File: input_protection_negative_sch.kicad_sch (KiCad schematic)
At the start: 26 parts, among them Q3 SQM50020EL, Q4 SQM50020EL, U2 LM5067

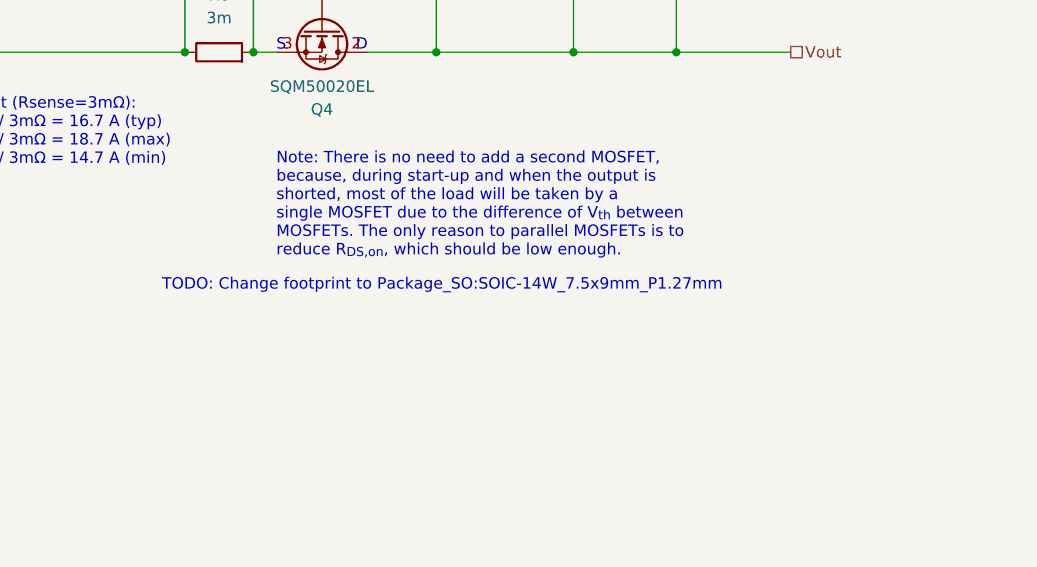
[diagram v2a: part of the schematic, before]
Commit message: Fixed LM5067 footprint
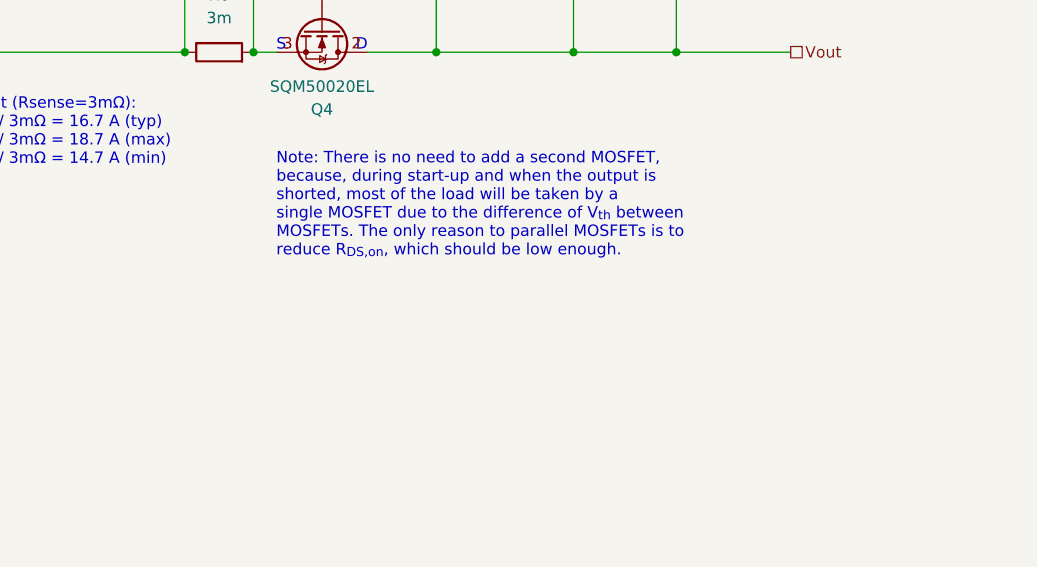
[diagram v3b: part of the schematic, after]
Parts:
- U2: footprint Package_SO:SOIC-14_3.9x8.7mm_P1.27mm -> Package_SO:SOIC-14W_7.5x9mm_P1.27mm
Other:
- note removed: "TODO: Change footprint to Package_SO:SOIC-14W_7.5x9mm_P1.27mm"
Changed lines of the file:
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@@
-    (effects (font (size 1.27 1.27)) (justify left bottom))
-  )
-  (text "TODO: Change footprint to Package_SO:SOIC-14W_7.5x9mm_P1.27mm"
-    (at 195.58 133.35 0)
     (effects (font (size 1.27 1.27)) (justify left bottom))
   )
@@
       (effects (font (size 1.27 1.27)))
     )
-    (property "Footprint" "Package_SO:SOIC-14_3.9x8.7mm_P1.27mm" (at 213.36 86.36 0)
-      (effects (font (size 1.27 1.27)) hide)
-    )
+    (property "Footprint" "Package_SO:SOIC-14W_7.5x9mm_P1.27mm" (at 213.36 86.36 0)
+      (effects (font (size 1.27 1.27)) hide)
+    )

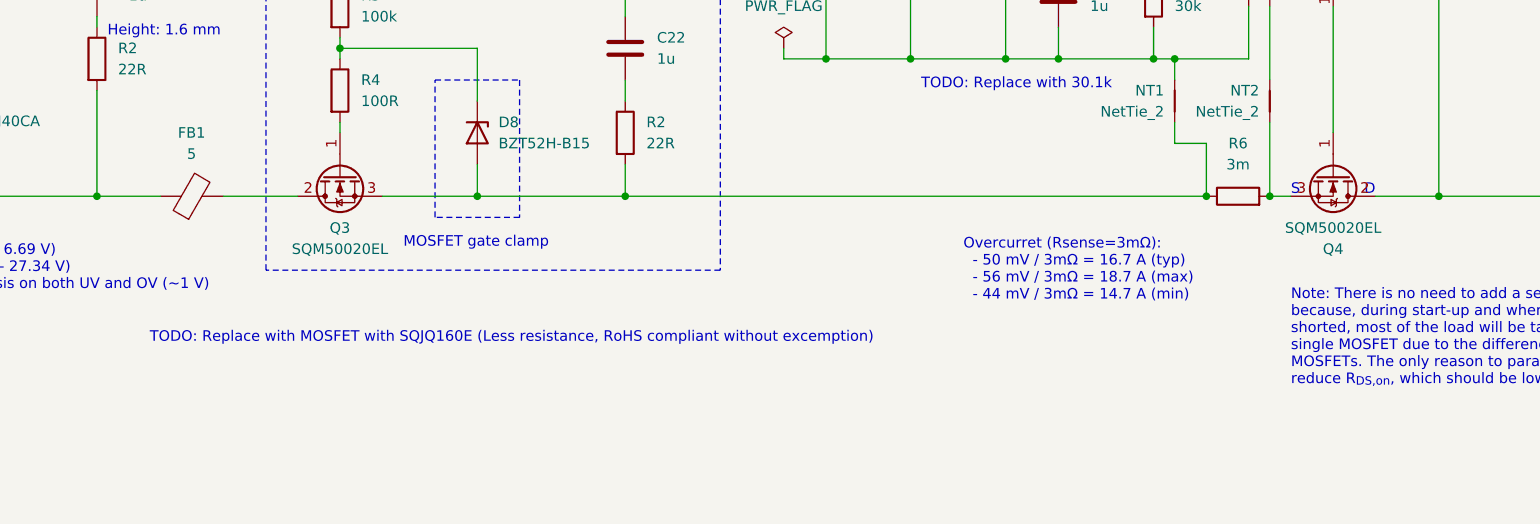
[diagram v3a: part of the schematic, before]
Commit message: Replace negative rail NMOS with SQJQ160E to reduce the on resistance
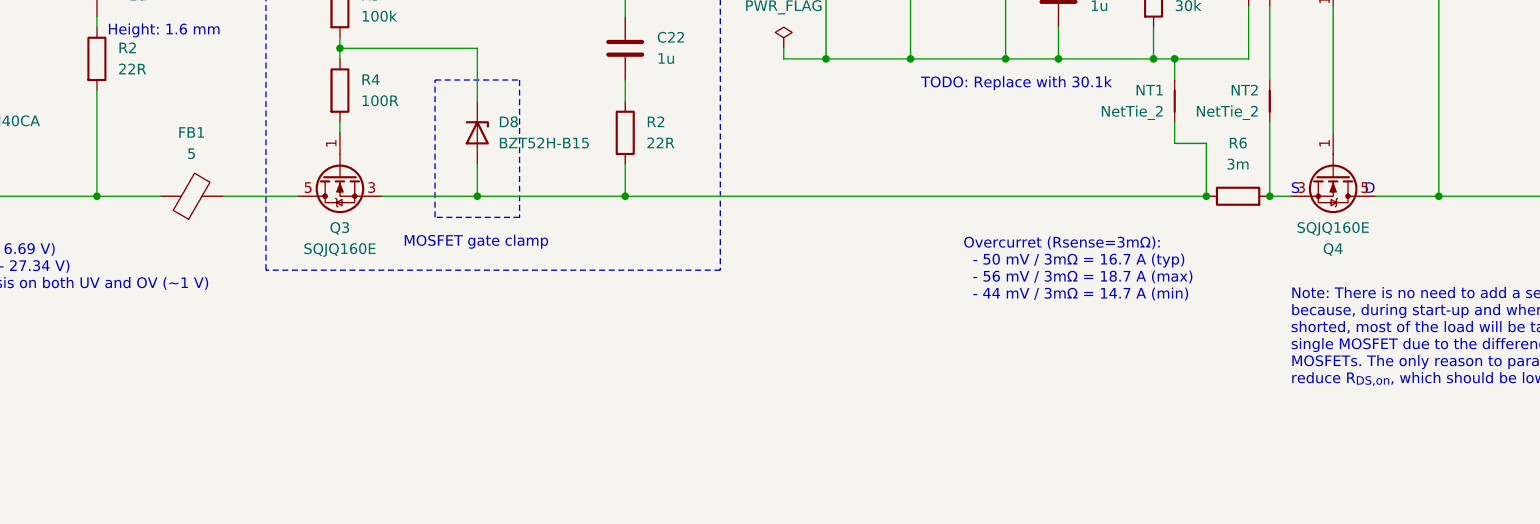
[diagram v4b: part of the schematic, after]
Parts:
- Q3, Q4: value SQM50020EL -> SQJQ160E; footprint Package_TO_SOT_SMD:TO-263-2 -> Package_SO:PowerPAK_SO-8L_Single; symbol Device:Q_NMOS_GDS -> Vishay:SQJQ160E; PN SQM50020EL -> SQJQ160E
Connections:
- net Vout: now also Q4.5 (D); no longer Q4.2 (D)
- net at NT2.1, Q4.3 (S), R6.2: now also Q4.2 (S), Q4.4 (S)
- net at D8.2 (A), NT1.1, Q3.3 (S)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: now also Q3.2 (S), Q3.4 (S)
- net at FB1.2: now also Q3.5 (D); no longer Q3.2 (D)
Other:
- note removed: "TODO: Replace with MOSFET with SQJQ160E (Less resistance, RoHS compliant without excemption)"
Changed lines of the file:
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@@
     (effects (font (size 1.27 1.27)) (justify right bottom))
-  )
-  (text "TODO: Replace with MOSFET with SQJQ160E (Less resistance, RoHS compliant without excemption)"
-    (at 71.12 124.46 0)
-    (effects (font (size 1.27 1.27)) (justify left bottom))
   )
   (text "Reverse polarity protection" (at 99.06 35.56 0)
@@
     (effects (font (size 1.27 1.27)) (justify right))
   )
-  (symbol (lib_id "Device:Q_NMOS_GDS") (at 213.36 104.14 270) (unit 1)
+  (symbol (lib_id "Vishay:SQJQ160E") (at 213.36 104.14 270) (unit 1)
     (in_bom yes) (on_board yes) (dnp no)
     (property "Reference" "Q4" (at 213.36 113.03 90)
       (effects (font (size 1.27 1.27)))
     )
-    (property "Value" "SQM50020EL" (at 213.36 110.49 90)
+    (property "Value" "SQJQ160E" (at 213.36 110.49 90)
       (effects (font (size 1.27 1.27)))
     )
-    (property "Footprint" "Package_TO_SOT_SMD:TO-263-2" (at 215.9 109.22 0)
+    (property "Footprint" "Package_SO:PowerPAK_SO-8L_Single" (at 215.9 109.22 0)
       (effects (font (size 1.27 1.27)) hide)
     )
@@
       (effects (font (size 1.27 1.27)) hide)
     )
-    (property "PN" "SQM50020EL" (at 213.36 104.14 0)
+    (property "PN" "SQJQ160E" (at 213.36 104.14 0)
       (effects (font (size 1.27 1.27)) hide)
     )
@@
     (pin "2")
     (pin "3")
+    (pin "3")
+    (pin "5")
+    (pin "4")
     (instances
       (project "main"
@@
     )
   )
-  (symbol (lib_id "Device:Q_NMOS_GDS") (at 93.98 104.14 90) (mirror x) (unit 1)
+  (symbol (lib_id "Vishay:SQJQ160E") (at 93.98 104.14 90) (mirror x) (unit 1)
     (in_bom yes) (on_board yes) (dnp no)
     (property "Reference" "Q3" (at 93.98 110.49 90)
       (effects (font (size 1.27 1.27)))
     )
-    (property "Value" "SQM50020EL" (at 93.98 113.03 90)
+    (property "Value" "SQJQ160E" (at 93.98 113.03 90)
       (effects (font (size 1.27 1.27)))
     )
-    (property "Footprint" "Package_TO_SOT_SMD:TO-263-2" (at 91.44 109.22 0)
+    (property "Footprint" "Package_SO:PowerPAK_SO-8L_Single" (at 91.44 109.22 0)
       (effects (font (size 1.27 1.27)) hide)
     )
@@
       (effects (font (size 1.27 1.27)) hide)
     )
-    (property "PN" "SQM50020EL" (at 93.98 104.14 0)
+    (property "PN" "SQJQ160E" (at 93.98 104.14 0)
       (effects (font (size 1.27 1.27)) hide)
     )
@@
     (pin "2")
     (pin "3")
-    (instances
-      (project "main"
+    (pin "3")
+    (pin "5")
+    (pin "4")
+    (instances
+      (project "main"

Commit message: Replaced negative side NMOS with SQJQ160E Reduced number of thermal spokes required to 1
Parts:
- renumbered C20 to C29, FB1 to FB2
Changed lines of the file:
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@@
         )
         (path "/b4ace06a-3ad4-479e-aaa4-d547ecf6903f/1acfc0a8-4adc-455e-9f2b-420811df0901"
-          (reference "C21") (unit 1)
+          (reference "C30") (unit 1)
         )
       )
@@
   (symbol (lib_id "Device:FerriteBead") (at 76.2 106.68 90) (unit 1)
     (in_bom yes) (on_board yes) (dnp no) (fields_autoplaced)
-    (property "Reference" "FB1" (at 76.1492 99.06 90)
+    (property "Reference" "FB2" (at 76.1492 99.06 90)
       (effects (font (size 1.27 1.27)))
     )
@@
       (project "main"
         (path "/b4ace06a-3ad4-479e-aaa4-d547ecf6903f/1acfc0a8-4adc-455e-9f2b-420811df0901"
-          (reference "FB1") (unit 1)
+          (reference "FB2") (unit 1)
         )
       )
@@
         )
         (path "/b4ace06a-3ad4-479e-aaa4-d547ecf6903f/1acfc0a8-4adc-455e-9f2b-420811df0901"
-          (reference "R3") (unit 1)
+          (reference "R12") (unit 1)
         )
       )
@@
         )
         (path "/b4ace06a-3ad4-479e-aaa4-d547ecf6903f/1acfc0a8-4adc-455e-9f2b-420811df0901"
-          (reference "C22") (unit 1)
+          (reference "C31") (unit 1)
         )
       )
@@
         )
         (path "/b4ace06a-3ad4-479e-aaa4-d547ecf6903f/1acfc0a8-4adc-455e-9f2b-420811df0901"
-          (reference "C4") (unit 1)
+          (reference "C18") (unit 1)
         )
       )
@@
   (symbol (lib_id "Device:C") (at 180.34 82.55 0) (unit 1)
     (in_bom yes) (on_board yes) (dnp no) (fields_autoplaced)
-    (property "Reference" "C20" (at 184.15 81.28 0)
+    (property "Reference" "C29" (at 184.15 81.28 0)
       (effects (font (size 1.27 1.27)) (justify left))
     )
@@
       (project "main"
         (path "/b4ace06a-3ad4-479e-aaa4-d547ecf6903f/1acfc0a8-4adc-455e-9f2b-420811df0901"
-          (reference "C20") (unit 1)
-        )
-      )
+          (reference "C29") (unit 1)
+        )
+      )

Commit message: Consolidated BOM
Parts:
- Q3, Q4: RoHS By exemption -> Yes
- R18: value 30k -> 30.1k; PN CRCW080530K0FKEA -> CRCW080530K1FKEA
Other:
- note removed: "TODO: Replace with 30.1k"
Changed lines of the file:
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@@
-    (effects (font (size 1.27 1.27)) (justify left bottom))
-  )
-  (text "TODO: Replace with 30.1k" (at 163.83 93.98 0)
     (effects (font (size 1.27 1.27)) (justify left bottom))
   )
@@
       (effects (font (size 1.27 1.27)) hide)
     )
-    (property "RoHS" "By exemption" (at 213.36 104.14 0)
+    (property "RoHS" "Yes" (at 213.36 104.14 0)
       (effects (font (size 1.27 1.27)) hide)
     )
@@
       (effects (font (size 1.27 1.27)) (justify left))
     )
-    (property "Value" "30k" (at 194.31 83.82 0)
+    (property "Value" "30.1k" (at 194.31 83.82 0)
       (effects (font (size 1.27 1.27)) (justify left))
     )
@@
       (effects (font (size 1.27 1.27)) hide)
     )
-    (property "PN" "CRCW080530K0FKEA" (at 191.77 82.55 0)
+    (property "PN" "CRCW080530K1FKEA" (at 191.77 82.55 0)
       (effects (font (size 1.27 1.27)) hide)
     )
@@
       (effects (font (size 1.27 1.27)) hide)
     )
-    (property "RoHS" "By exemption" (at 93.98 104.14 0)
-      (effects (font (size 1.27 1.27)) hide)
-    )
+    (property "RoHS" "Yes" (at 93.98 104.14 0)
+      (effects (font (size 1.27 1.27)) hide)
+    )

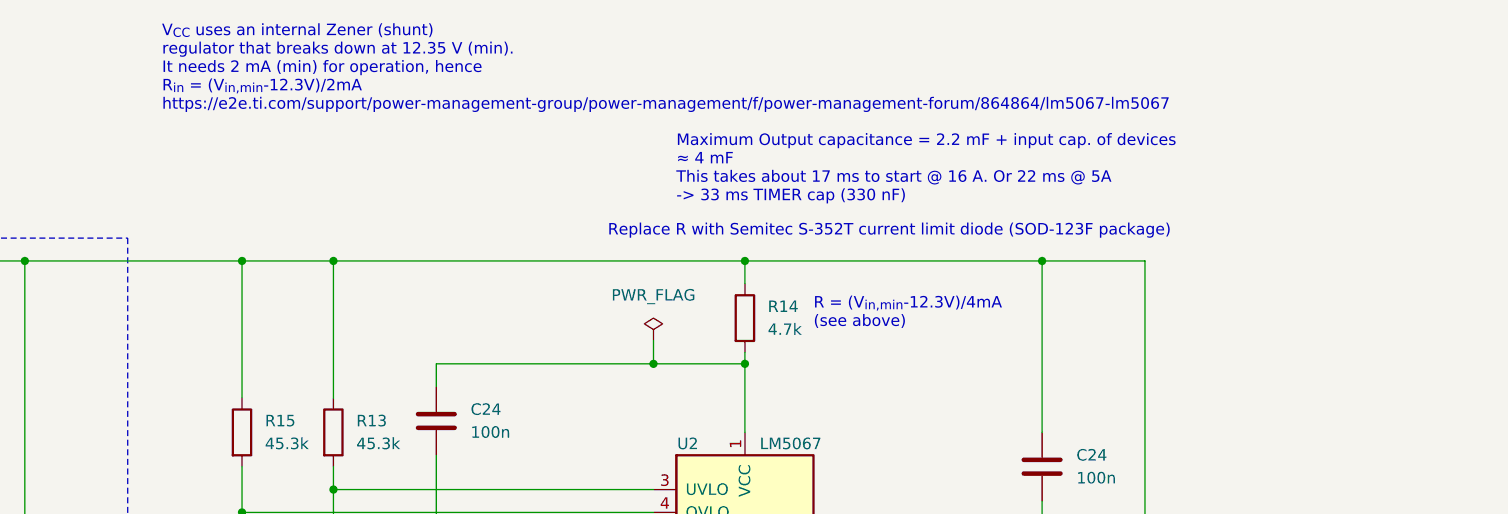
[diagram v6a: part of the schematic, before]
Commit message: Replaced LM5067 current limiting resistor with a current limiting diode to increase input voltage range
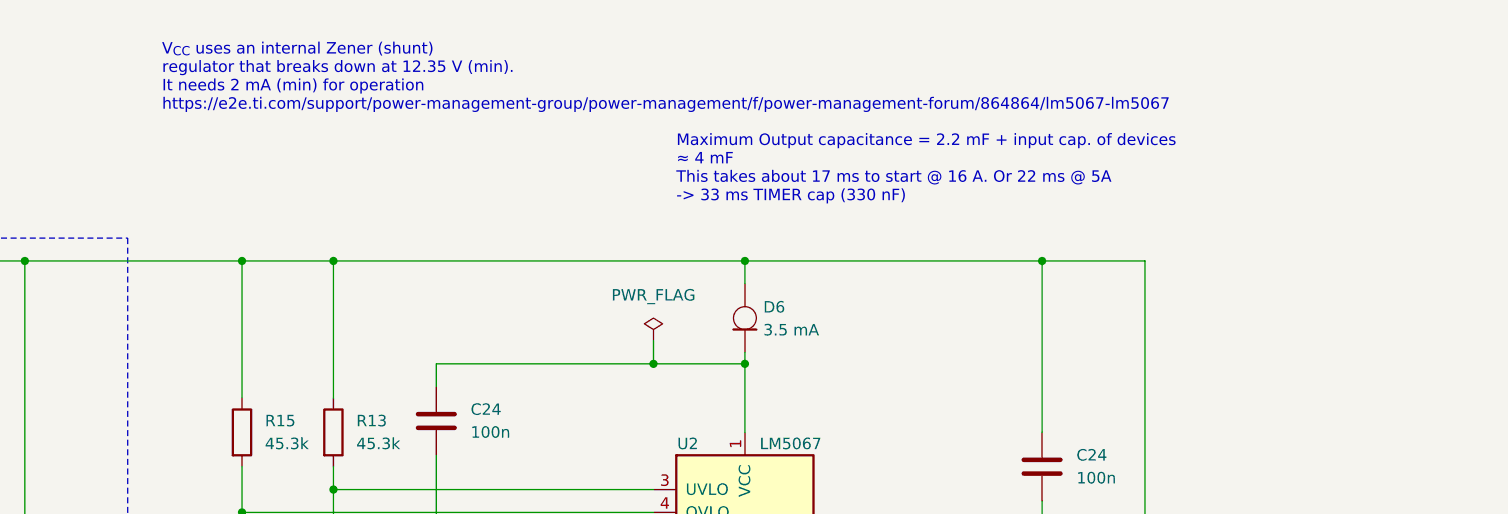
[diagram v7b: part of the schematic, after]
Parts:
- removed R14: 4.7k, Resistor_SMD:R_0805_2012Metric, symbol Device:R
- added D6: 3.5 mA, Diode_SMD:D_SOD-123F, symbol constant_current_diode:D_Constant_Current
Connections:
- net GND: now also D6.2 (A)
- net at C24.1, U2.1 (VCC): now also D6.1 (K)
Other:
- note added: "V_{CC} uses an internal Zener (shunt) regulator that breaks down at 12.35 V (min). It needs 2 mA (min) for operation https://e2e.ti.com/support/power-management-group/power-management/f/power-management-forum/864864/lm5067-lm5067"
- note removed: "R = (V_{in,min}-12.3V)/4mA (see above)"
- note removed: "Replace R with Semitec S-352T current limit diode (SOD-123F package)"
- note removed: "V_{CC} uses an internal Zener (shunt) regulator that breaks down at 12.35 V (min). It needs 2 mA (min) for operation, hence R_{in} = (V_{in,min}-12.3V)/2mA https://e2e.ti.com/support/power-management-group/power-management/f/power-management-forum/864864/lm5067-lm5067"
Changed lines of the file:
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@@
-    (effects (font (size 1.27 1.27)) (justify left bottom))
-  )
-  (text "Replace R with Semitec S-352T current limit diode (SOD-123F package)"
-    (at 193.04 36.83 0)
     (effects (font (size 1.27 1.27)) (justify left bottom))
   )
@@
     (effects (font (size 1.27 1.27)) (justify left bottom))
   )
-  (text "V_{CC} uses an internal Zener (shunt)\nregulator that breaks down at 12.35 V (min).\nIt needs 2 mA (min) for operation, hence\nR_{in} = (V_{in,min}-12.3V)/2mA\nhttps://e2e.ti.com/support/power-management-group/power-management/f/power-management-forum/864864/lm5067-lm5067\n"
+  (text "V_{CC} uses an internal Zener (shunt)\nregulator that breaks down at 12.35 V (min).\nIt needs 2 mA (min) for operation\nhttps://e2e.ti.com/support/power-management-group/power-management/f/power-management-forum/864864/lm5067-lm5067\n"
     (at 143.51 22.86 0)
     (effects (font (size 1.27 1.27)) (justify left bottom))
@@
   (text "Overcurret (Rsense=3mΩ):\n  - 50 mV / 3mΩ = 16.7 A (typ)\n  - 56 mV / 3mΩ = 18.7 A (max)\n  - 44 mV / 3mΩ = 14.7 A (min)"
     (at 168.91 119.38 0)
-    (effects (font (size 1.27 1.27)) (justify left bottom))
-  )
-  (text "R = (V_{in,min}-12.3V)/4mA\n(see above)" (at 215.9 46.99 0)
     (effects (font (size 1.27 1.27)) (justify left bottom))
   )
@@
     )
   )
-  (symbol (lib_id "Device:R") (at 208.28 45.72 0) (unit 1)
-    (in_bom yes) (on_board yes) (dnp no) (fields_autoplaced)
-    (property "Reference" "R14" (at 210.82 44.45 0)
-      (effects (font (size 1.27 1.27)) (justify left))
-    )
-    (property "Value" "4.7k" (at 210.82 46.99 0)
-      (effects (font (size 1.27 1.27)) (justify left))
-    )
-    (property "Footprint" "Resistor_SMD:R_0805_2012Metric" (at 206.502 45.72 90)
-      (effects (font (size 1.27 1.27)) hide)
-    )
-    (property "Datasheet" "~" (at 208.28 45.72 0)
-      (effects (font (size 1.27 1.27)) hide)
-    )
-    (property "MFN" "Vishay" (at 208.28 45.72 0)
-      (effects (font (size 1.27 1.27)) hide)
-    )
-    (property "PN" "CRCW08054K70FKEA" (at 208.28 45.72 0)
-      (effects (font (size 1.27 1.27)) hide)
-    )
-    (property "Temperature" "Tstorage = –55 °C to 155 °C" (at 208.28 45.72 0)
-      (effects (font (size 1.27 1.27)) hide)
-    )
-    (property "RoHS" "By exemption" (at 208.28 45.72 0)
-      (effects (font (size 1.27 1.27)) hide)
-    )
-    (property "Note" "1%, 150 V" (at 208.28 45.72 0)
-      (effects (font (size 1.27 1.27)) hide)
-    )
-    (pin "1")
-    (pin "2")
-    (instances
-      (project "main"
-        (path "/b4ace06a-3ad4-479e-aaa4-d547ecf6903f/1acfc0a8-4adc-455e-9f2b-420811df0901"
-          (reference "R14") (unit 1)
-        )
-      )
-    )
-  )
   (symbol (lib_id "Device:NetTie_2") (at 194.31 95.25 270) (mirror x) (unit 1)
     (in_bom no) (on_board yes) (dnp no)
@@
         )
       )
+    )
+  )
+  (symbol (lib_id "constant_current_diode:D_Constant_Current") (at 208.28 45.72 90) (unit 1)
+    (in_bom yes) (on_board yes) (dnp no) (fields_autoplaced)
+    (property "Reference" "D6" (at 210.312 44.5135 90)
+      (effects (font (size 1.27 1.27)) (justify right))
+    )
+    (property "Value" "3.5 mA" (at 210.312 47.0535 90)
+      (effects (font (size 1.27 1.27)) (justify right))
+    )
+    (property "Footprint" "Diode_SMD:D_SOD-123F" (at 208.28 45.72 0)
+      (effects (font (size 1.27 1.27)) hide)
+    )
+    (property "Datasheet" "~" (at 208.28 45.72 0)
+      (effects (font (size 1.27 1.27)) hide)
+    )
+    (property "MFN" "Semitec" (at 208.28 45.72 0)
+      (effects (font (size 1.27 1.27)) hide)
+    )
+    (property "PN" "S-352T" (at 208.28 45.72 0)
+      (effects (font (size 1.27 1.27)) hide)
+    )
+    (pin "1")
+    (pin "2")
+    (instances
+      (project "main"
+        (path "/b4ace06a-3ad4-479e-aaa4-d547ecf6903f/1acfc0a8-4adc-455e-9f2b-420811df0901"
+          (reference "D6") (unit 1)
+        )
+      )
